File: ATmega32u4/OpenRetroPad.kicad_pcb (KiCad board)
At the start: 2 copper layers, 46 x 74 mm, 45 parts, among them J1 USB_B_Micro, J2 NRF24, J3 DB25_Female_MountingHoles, SW1 SW_Push, SW2 SW_Push, U1 ATmega32U4, U2 AMS1117-3.3, Y1 16MHz

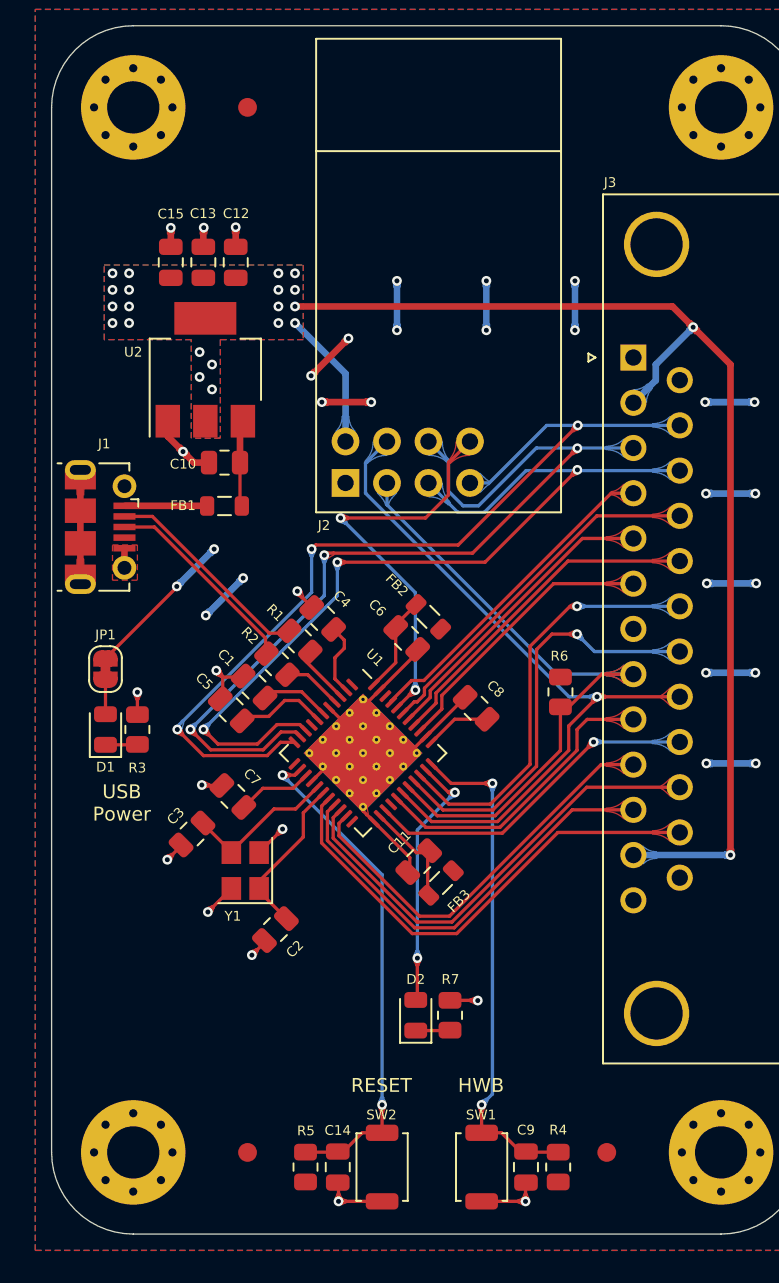
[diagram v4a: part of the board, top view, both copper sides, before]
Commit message: - Add on-board programmer - Micro USB -> USB-C
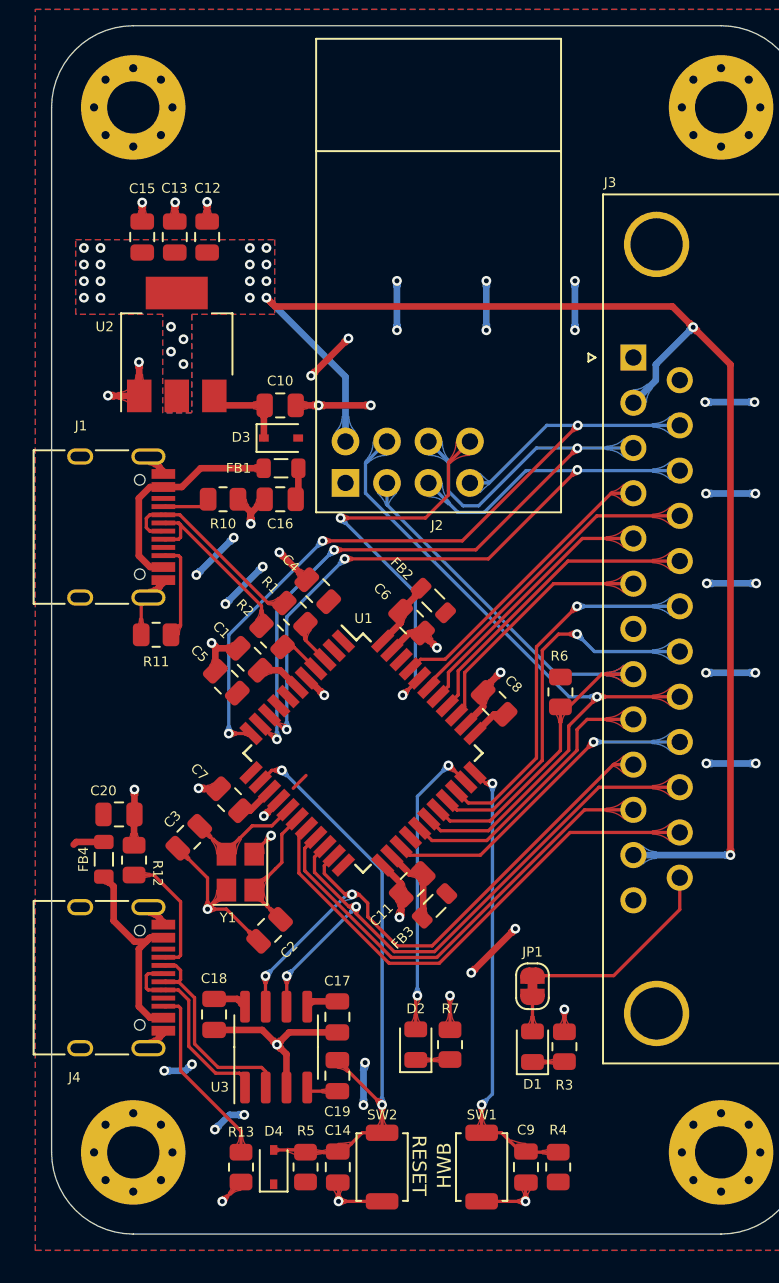
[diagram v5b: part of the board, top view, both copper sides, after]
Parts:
- removed FID1, FID2, FID3: Fiducial, OpenRetroPad:Fiducial_JLCPCB
- added C16: 10u, Capacitor_SMD:C_0805_2012Metric, F.Cu at (120.8, 86.2)
- added C17: 100n, Capacitor_SMD:C_0805_2012Metric, F.Cu at (124.3, 117.9)
- added C18: 100n, Capacitor_SMD:C_0805_2012Metric, F.Cu at (116.7, 117.8)
- added C19: 100n, Capacitor_SMD:C_0805_2012Metric, F.Cu at (124.3, 121.5)
- added C20: 10u, Capacitor_SMD:C_0805_2012Metric, F.Cu at (110.9, 105.5)
- added D3: 1N5817, Diode_SMD:D_SOD-323, F.Cu at (120.8, 82.5)
- added D4: 1N5817, Diode_SMD:D_SOD-323, F.Cu at (120.4, 127.1)
- added FB4: 500mA, Inductor_SMD:L_0805_2012Metric, F.Cu at (110.0, 108.3)
- added J4: USB_C_Receptacle_USB2.0, Connector_USB:USB_C_Receptacle_HRO_TYPE-C-31-M-12, F.Cu at (109.6, 115.5)
- added R10: 5.1k, Resistor_SMD:R_0805_2012Metric, F.Cu at (117.3, 86.2)
- added R11: 5.1k, Resistor_SMD:R_0805_2012Metric, F.Cu at (113.2, 94.5)
- added R12: 5.1k, Resistor_SMD:R_0805_2012Metric, F.Cu at (111.8, 108.3)
- added R13: 5.1k, Resistor_SMD:R_0805_2012Metric, F.Cu at (118.4, 127.1)
- added U3: CH330N, Package_SO:SOIC-8_3.9x4.9mm_P1.27mm, F.Cu at (120.5, 119.8)
- J1: value USB_B_Micro -> USB_C_Receptacle_USB2.0; footprint OpenRetroPad:105017-0001 -> Connector_USB:USB_C_Receptacle_HRO_TYPE-C-31-M-12
- U1: footprint Package_DFN_QFN:QFN-44-1EP_7x7mm_P0.5mm_EP5.15x5.15mm_ThermalVias -> Package_QFP:TQFP-44_10x10mm_P0.8mm
- moved JP1 32.6 mm to (136.2, 116.1)
- moved D1 32.6 mm to (136.2, 119.8)
- moved R3 32.6 mm to (138.2, 119.8)
- moved C10 4.89 mm to (120.8, 80.5), turned to 180 degrees
- moved FB1 4.16 mm to (120.8, 84.3)
- moved C12 2.34 mm to (116.3, 70.2)
- moved C13 2.34 mm to (114.3, 70.2)
- moved C15 2.34 mm to (112.3, 70.2)
- moved U2 2.34 mm to (114.4, 76.8)
- moved D2 1.80 mm to (129.1, 119.6)
- moved R7 1.80 mm to (131.2, 119.6)
- moved C1 1.73 mm to (118.9, 96.0)
- moved C4 1.73 mm to (123.1, 91.8)
- moved R1 1.73 mm to (121.7, 93.2)
- moved R2 1.73 mm to (120.3, 94.6)
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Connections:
- C10 pad 2: +5V -> Net-(C10-Pad2)
- R1 pad 2: D- -> MCU_D-
- R2 pad 2: D+ -> MCU_D+
- U2 pad 3: +5V -> Net-(C10-Pad2)
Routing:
- net GND: track 73.9 -> 92.9 mm, vias 19 -> 29
- net /UART_D-: track 0.00 -> 14.0 mm
- net D-: track 13.1 -> 0.00 mm
- net Net-(FB4-Pad2): track 0.00 -> 12.9 mm
- net D+: track 12.5 -> 0.00 mm
- net MCU_D-: track 0.00 -> 12.5 mm
- net /UART_D+: track 0.00 -> 12.4 mm
- net Net-(J4-PadB5): track 0.00 -> 11.5 mm
- net MCU_D+: track 0.00 -> 11.4 mm
- net PD3: track 25.3 -> 36.4 mm, vias 0 -> 2
- net PD2: track 28.7 -> 38.5 mm, vias 0 -> 2
- net Net-(FB1-Pad2): track 5.04 -> 14.1 mm
- net PB2: track 56.9 -> 48.7 mm
- net PB1: track 55.2 -> 47.0 mm
- net PB3: track 56.4 -> 48.4 mm
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- removed copper zone on F.Cu, net GND
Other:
- board text added: "OpenRetroPad ATmega32u4 v1 MAY-2021 OpenRetroPad.com JLCJLCJLCJLC"
- board text removed: "- - - D14 D16 D15 D23 D21 D20 D19 D18 D5 - D10 D9 D8 D6 D4 D1 D0 D2 D3 - - -"
- board text removed: "- - - MISO MOSI SCK A5 A3 A2 A1 A0 - - A10 A9 A8 A7 A6 TX RX SDA SCL - - -"
- board text removed: "Alt"
- board text removed: "Leonardo"
- board text removed: "OpenRetroPad ATmega32u4 v1 JAN-2021 OpenRetroPad.com"
- board text removed: "USB Power"

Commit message: Update V2
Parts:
- added D5: 1N5817, Diode_SMD:D_SOD-323, F.Cu at (105.5, 141.5)
- added D6: Power, LED_SMD:LED_0603_1608Metric, F.Cu at (98.2, 138.7)
- added D7: RX, LED_SMD:LED_0603_1608Metric, F.Cu at (121.9, 154.4)
- added D8: TX, LED_SMD:LED_0603_1608Metric, F.Cu at (123.5, 154.4)
- added F1: 500mA, Fuse:Fuse_0805_2012Metric, F.Cu at (121.6, 109.2)
- added F2: 500mA, Fuse:Fuse_0805_2012Metric, F.Cu at (121.6, 113.5)
- added R14: 1k, Resistor_SMD:R_0603_1608Metric, F.Cu at (121.9, 150.0)
- added R15: 1k, Resistor_SMD:R_0603_1608Metric, F.Cu at (123.5, 150.0)
- added R16: 330, Resistor_SMD:R_0603_1608Metric, F.Cu at (115.5, 161.4)
- added R8: 1k, Resistor_SMD:R_0603_1608Metric, F.Cu at (118.3, 150.0)
- added R9: 330, Resistor_SMD:R_0603_1608Metric, F.Cu at (120.5, 161.4)
- added U4: USBLC6-2SC6, Package_TO_SOT_SMD:SOT-23-6, F.Cu at (106.1, 126.0)
- added U5: USBLC6-2SC6, Package_TO_SOT_SMD:SOT-23-6, F.Cu at (106.0, 153.4)
- C1: value 1u -> 10u
- C10, C16, C20: value 10u -> 100n; footprint Capacitor_SMD:C_0805_2012Metric -> Capacitor_SMD:C_0603_1608Metric
- C11: value 100n -> 20pF; footprint Capacitor_SMD:C_0805_2012Metric -> Capacitor_SMD:C_0603_1608Metric
- C12: value 10u -> 20pF; footprint Capacitor_SMD:C_0805_2012Metric -> Capacitor_SMD:C_0603_1608Metric
- C13, C15, C17, C18, C19, C4, C8, C9: footprint Capacitor_SMD:C_0805_2012Metric -> Capacitor_SMD:C_0603_1608Metric
- C14, C7: value 100n -> 1u; footprint Capacitor_SMD:C_0805_2012Metric -> Capacitor_SMD:C_0603_1608Metric
- C2, C3: value 20pF -> 10u
- C5: value 1u -> 100n; footprint Capacitor_SMD:C_0805_2012Metric -> Capacitor_SMD:C_0603_1608Metric
- C6: value 100n -> 10u
- D1: value Power LED -> 1N5817; footprint LED_SMD:LED_0805_2012Metric -> Diode_SMD:D_SOD-323
- D2: value LED1 -> TX; footprint LED_SMD:LED_0805_2012Metric -> LED_SMD:LED_0603_1608Metric
- D3: value 1N5817 -> RX; footprint Diode_SMD:D_SOD-323 -> LED_SMD:LED_0603_1608Metric
- D4: value 1N5817 -> User; footprint Diode_SMD:D_SOD-323 -> LED_SMD:LED_0603_1608Metric
- FB3, FB4: footprint Inductor_SMD:L_0805_2012Metric -> Inductor_SMD:L_0603_1608Metric
- H1, H2, H3, H4: value 3.2mm_M3 -> 3.2mm M3
- J2: value NRF24 -> USB_C_Receptacle_USB2.0; footprint OpenRetroPad:NRF24L01 -> Connector_USB:USB_C_Receptacle_HRO_TYPE-C-31-M-12
- J3: value DB25_Female_MountingHoles -> NRF24; footprint Connector_Dsub:DSUB-25_Female_Horizontal_P2.77x2.84mm_EdgePinOffset7.70mm_Housed_MountingHolesOffset9.12mm -> OpenRetroPad:NRF24L01
- J4: value USB_C_Receptacle_USB2.0 -> DB25_Male_MountingHoles; footprint Connector_USB:USB_C_Receptacle_HRO_TYPE-C-31-M-12 -> Connector_Dsub:DSUB-25_Male_Horizontal_P2.77x2.84mm_EdgePinOffset7.70mm_Housed_MountingHolesOffset9.12mm
- R1, R2: value 22r -> 5.1k; footprint Resistor_SMD:R_0805_2012Metric -> Resistor_SMD:R_0603_1608Metric
- R10, R12, R13: value 5.1k -> 1k; footprint Resistor_SMD:R_0805_2012Metric -> Resistor_SMD:R_0603_1608Metric
- R11: value 5.1k -> 10k; footprint Resistor_SMD:R_0805_2012Metric -> Resistor_SMD:R_0603_1608Metric
- R3: value 1k -> 5.1k; footprint Resistor_SMD:R_0805_2012Metric -> Resistor_SMD:R_0603_1608Metric
- R4: value 10k -> 5.1k; footprint Resistor_SMD:R_0805_2012Metric -> Resistor_SMD:R_0603_1608Metric
- R5: value 10k -> 22r; footprint Resistor_SMD:R_0805_2012Metric -> Resistor_SMD:R_0603_1608Metric
- R6: value 1k -> 22r; footprint Resistor_SMD:R_0805_2012Metric -> Resistor_SMD:R_0603_1608Metric
- R7: footprint Resistor_SMD:R_0805_2012Metric -> Resistor_SMD:R_0603_1608Metric
- SW1: value SW_Push -> HWB
- SW2: value SW_Push -> RESET
- U1: value ATmega32U4 -> AMS1117-3.3; footprint Package_QFP:TQFP-44_10x10mm_P0.8mm -> Package_TO_SOT_SMD:SOT-223-3_TabPin2
- U2: value AMS1117-3.3 -> ATmega32U4-M; footprint Package_TO_SOT_SMD:SOT-223-3_TabPin2 -> Package_QFP:TQFP-44_10x10mm_P0.8mm
- moved H2 112.4 mm to (100.0, 164.0)
- moved C15 79.9 mm to (115.2, 150.0), turned to 90 degrees
- moved C12 74.0 mm to (107.7, 143.7), turned to -135 degrees
- moved J2 73.2 mm to (97.8, 153.3), turned to -90 degrees
- moved D3 72.0 mm to (118.3, 154.4), turned to -90 degrees
- moved C16 65.0 mm to (108.2, 150.0), turned to 90 degrees
- moved C10 64.4 mm to (122.5, 144.9), turned to 135 degrees
- moved FB2 63.0 mm to (104.0, 149.7), turned to 90 degrees
- moved C13 60.6 mm to (110.4, 130.7), turned to -45 degrees
- moved U2 59.4 mm to (118.0, 136.0), turned to -45 degrees
- moved C6 59.1 mm to (103.0, 146.9), turned to 0 degrees
- moved R10 56.1 mm to (125.6, 141.8), turned to 135 degrees
- moved J3 53.9 mm to (112.9, 122.7)
- moved R3 49.7 mm to (104.6, 156.4), turned to 0 degrees
- moved LOGO1 46.3 mm to (109.1, 164.1)
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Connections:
- C1 pad 2: Net-(C1-Pad2) -> +5V
- C10 pad 2: Net-(C10-Pad2) -> /Microcontroller/AVCC_P24
- C11 pad 1: GND -> /Microcontroller/XTAL1
- C11 pad 2: Net-(C11-Pad2) -> GND
- C12 pad 1: GND -> /Microcontroller/XTAL2
- C12 pad 2: +3V3 -> GND
- C13 pad 2: +3V3 -> /Microcontroller/UCAP
- C14 pad 1: RESET -> GND
- C14 pad 2: GND -> /Microcontroller/UGND
- C15 pad 2: +3V3 -> +5V
- C16 pad 2: +5V -> /UART/V3
- C17 pad 1: GND -> /UART/RTS
- C17 pad 2: +5V -> /DB25/RST
- C18 pad 2: Net-(C18-Pad2) -> /Microcontroller/AVCC_P44
- C19 pad 1: Net-(C19-Pad1) -> /DB25/RST
- C19 pad 2: RESET -> GND
- C2 pad 1: XTAL1 -> GND
- C2 pad 2: GND -> /Power/VREGIN
- C3 pad 1: XTAL2 -> GND
- C3 pad 2: GND -> +3V3
- C4 pad 2: +5V -> +3V3
- C5 pad 2: +5V -> +3V3
- C6 pad 2: Net-(C6-Pad2) -> +5V
- C9 pad 1: PE2 -> GND
- C9 pad 2: GND -> +5V
- D1 pad 1: Net-(D1-Pad1) -> /Power/VREGIN
- D1 pad 2: Net-(D1-Pad2) -> +5V
- D2 pad 2: PC7 -> +5V
- D3 pad 1: Net-(C10-Pad2) -> Net-(D3-Pad1)
- D4 pad 1: +5V -> Net-(D4-Pad1)
- D4 pad 2: RESET -> /IO/LED_USER
- FB1 pad 1: +5V -> /USB Data/VBUS
- FB1 pad 2: Net-(FB1-Pad2) -> +5V
- FB2 pad 1: +5V -> /USB Program/VBUS
- FB2 pad 2: Net-(C6-Pad2) -> +5V
- FB3 pad 1: +5V -> /Microcontroller/AVCC_P24
- FB3 pad 2: Net-(C11-Pad2) -> +5V
- FB4 pad 1: +5V -> /Microcontroller/AVCC_P44
- FB4 pad 2: Net-(FB4-Pad2) -> +5V
- H1 pad 1: (no net) -> unconnected-(H1-Pad1)
- H2 pad 1: (no net) -> unconnected-(H2-Pad1)
- H3 pad 1: (no net) -> unconnected-(H3-Pad1)
- H4 pad 1: (no net) -> unconnected-(H4-Pad1)
- J1 pad A4: Net-(FB1-Pad2) -> /USB Data/VBUS
- J1 pad A5: Net-(J1-PadA5) -> /USB Data/CC1
- J1 pad A6: MCU_D+ -> /USB Data/D+
- J1 pad A7: MCU_D- -> /USB Data/D-
- J1 pad A8: Net-(J1-PadA8) -> unconnected-(J1-PadA8)
- J1 pad A9: Net-(FB1-Pad2) -> /USB Data/VBUS
- J1 pad B4: Net-(FB1-Pad2) -> /USB Data/VBUS
- J1 pad B5: Net-(J1-PadB5) -> /USB Data/CC2
- J1 pad B6: MCU_D+ -> /USB Data/D+
- J1 pad B7: MCU_D- -> /USB Data/D-
- J1 pad B8: Net-(J1-PadB8) -> unconnected-(J1-PadB8)
- J1 pad B9: Net-(FB1-Pad2) -> /USB Data/VBUS
- J3 pad 3: PB2 -> /DB25/CE
- J3 pad 4: PF0 -> /DB25/CSN
- J3 pad 5: PF5 -> /DB25/SCK
- J3 pad 6: PF7 -> /DB25/MOSI
- J3 pad 7: Net-(J3-Pad7) -> /DB25/MISO
- J3 pad 8: PB5 -> /DB25/IRQ
- JP1 pad 2: Net-(D1-Pad2) -> Net-(D6-Pad2)
- R1 pad 1: Net-(R1-Pad1) -> /USB Data/CC2
- R1 pad 2: MCU_D- -> GND
- R10 pad 2: Net-(J1-PadA5) -> Net-(D4-Pad1)
- R11 pad 1: Net-(J1-PadB5) -> +5V
- R11 pad 2: GND -> /DB25/RST
- R12 pad 1: GND -> /DB25/PB5
- R12 pad 2: Net-(J4-PadA5) -> +5V
- R13 pad 1: Net-(J4-PadB5) -> Net-(D6-Pad1)
- R2 pad 1: Net-(R2-Pad1) -> GND
- R2 pad 2: MCU_D+ -> /USB Data/CC1
- R3 pad 1: Net-(D1-Pad1) -> /USB Program/CC2
- R4 pad 1: +5V -> GND
- R4 pad 2: PE2 -> /USB Program/CC1
- R5 pad 1: +5V -> /Microcontroller/D+
- R5 pad 2: RESET -> /Microcontroller/USB_DATA.DP
- R6 pad 1: PB5 -> /Microcontroller/D-
- R6 pad 2: +5V -> /Microcontroller/USB_DATA.DM
- R7 pad 1: GND -> Net-(D2-Pad1)
- R7 pad 2: Net-(D2-Pad1) -> /DB25/TX
- SW1 pad 1: PE2 -> Net-(R9-Pad2)
- SW2 pad 1: RESET -> Net-(R16-Pad2)
- U1 pad 1: Net-(U1-Pad1) -> GND
- U1 pad 2: +5V -> +3V3
- U1 pad 3: Net-(R1-Pad1) -> /Power/VREGIN
- U2 pad 1: GND -> /DB25/CE
- U2 pad 2: +3V3 -> +5V
- U2 pad 3: Net-(C10-Pad2) -> /Microcontroller/D-
- U3 pad 1: /UART_D+ -> /UART/USB_PRGM.DP
- U3 pad 2: /UART_D- -> /UART/USB_PRGM.DM
- U3 pad 4: Net-(C19-Pad1) -> /UART/RTS
- U3 pad 6: PD2 -> /DB25/TX
- U3 pad 7: PD3 -> /DB25/RX
- U3 pad 8: Net-(C18-Pad2) -> /UART/V3
- Y1 pad 1: XTAL1 -> /Microcontroller/XTAL1
- Y1 pad 3: XTAL2 -> /Microcontroller/XTAL2
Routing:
- net +3V3: track 83.6 -> 30.2 mm, vias 22 -> 26
- net PB2: track 48.7 -> 0.00 mm, vias 3 -> 0
- net PB3: track 48.4 -> 0.00 mm, vias 3 -> 0
- net PB1: track 47.0 -> 0.00 mm, vias 3 -> 0
- net /DB25/MISO: track 0.00 -> 45.7 mm, vias 0 -> 2
- net /DB25/RX: track 0.00 -> 43.7 mm, vias 0 -> 1
- net PB4: track 43.0 -> 0.00 mm, vias 1 -> 0
- net /DB25/MOSI: track 0.00 -> 42.1 mm, vias 0 -> 1
- net /DB25/SCK: track 0.00 -> 39.7 mm, vias 0 -> 1
- net PD2: track 38.5 -> 0.00 mm, vias 2 -> 0
- net PB5: track 38.3 -> 0.00 mm
- net RESET: track 37.7 -> 0.00 mm, vias 2 -> 0
- net /DB25/RST: track 0.00 -> 37.6 mm, vias 0 -> 4
- net PD3: track 36.4 -> 0.00 mm, vias 2 -> 0
- net /DB25/TX: track 0.00 -> 32.4 mm, vias 0 -> 3
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- added copper zone on In2.Cu, net +5V
- added copper zone on F.Cu, net GND
- added copper zone on In1.Cu, net GND
- removed copper zone on B.Cu, net GND
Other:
- copper layers 2 -> 4
- net class Default removed
- board text added: "DATA"
- board text added: "OpenRetroPad ATmega32u4 v2 DEC-2022 OpenRetroPad.com JLCJLCJLCJLC"
- board text added: "POWER"
- board text added: "PRGM"
- board text added: "RX TX"
- board text added: "TX RX"
- board text added: "UART"
- board text added: "USB"
- board text added: "USER"
- board text removed: "1 14 2 15 3 16 4 17 5 18 6 19 7 20 8 21 9 22 10 23 11 24 12 25 13"
- board text removed: "3V3 GND"
- board text removed: "ATmega32u4"
- board text removed: "DB25"
- board text removed: "GND 5V 3V3 PB3 PB2 PB1 PF0 PF4 PF5 PF6 PF7 PC6 - PB6 PB5 PB4 PD7 PD4 PD3 PD2 PD1 PD0 3V3 5V GND"
- board text removed: "OpenRetroPad ATmega32u4 v1 MAY-2021 OpenRetroPad.com JLCJLCJLCJLC"
- board text removed: "PB2 PB1"
- board text removed: "PB4 PB5"
- board text removed: "PF1 PB3"

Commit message: Update layout/assembly pdf
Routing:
- net /DB25/PD0: track 28.9 -> 27.5 mm
- net /Microcontroller/USB_DATA.DP: track 5.14 -> 6.22 mm
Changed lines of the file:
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@@
   (segment (start 116.15 143.506854) (end 116.797918 142.858936) (width 0.2032) (layer "F.Cu") (net 17))
   (segment (start 123.017053 149.175) (end 121.492053 147.65) (width 0.2032) (layer "F.Cu") (net 17))
-  (segment (start 110.928678 126.95) (end 111.955976 127.977298) (width 0.2032) (layer "F.Cu") (net 20))
-  (segment (start 107.2375 126.95) (end 110.928678 126.95) (width 0.2032) (layer "F.Cu") (net 20))
-  (segment (start 107.2375 125.05) (end 111.15 125.05) (width 0.2032) (layer "F.Cu") (net 21))
-  (segment (start 111.15 125.05) (end 113.016637 126.916637) (width 0.2032) (layer "F.Cu") (net 21))
+  (segment (start 108.271342 126.2) (end 110.95 126.2) (width 0.2032) (layer "F.Cu") (net 20))
+  (segment (start 110.95 126.2) (end 111.955976 127.205976) (width 0.2032) (layer "F.Cu") (net 20))
+  (segment (start 107.521342 126.95) (end 108.271342 126.2) (width 0.2032) (layer "F.Cu") (net 20))
+  (segment (start 111.955976 127.205976) (end 111.955976 127.977298) (width 0.2032) (layer "F.Cu") (net 20))
+  (segment (start 107.2375 126.95) (end 107.521342 126.95) (width 0.2032) (layer "F.Cu") (net 20))
+  (segment (start 108.221342 125.75) (end 111.1 125.75) (width 0.2032) (layer "F.Cu") (net 21))
+  (segment (start 112.266637 126.916637) (end 113.016637 126.916637) (width 0.2032) (layer "F.Cu") (net 21))
+  (segment (start 107.521342 125.05) (end 108.221342 125.75) (width 0.2032) (layer "F.Cu") (net 21))
+  (segment (start 107.2375 125.05) (end 107.521342 125.05) (width 0.2032) (layer "F.Cu") (net 21))
+  (segment (start 111.1 125.75) (end 112.266637 126.916637) (width 0.2032) (layer "F.Cu") (net 21))
   (segment (start 116.7 150.825) (end 116.7 153.6125) (width 0.2032) (layer "F.Cu") (net 22))
-  (segment (start 107.1375 154.35) (end 109.795 154.35) (width 0.2032) (layer "F.Cu") (net 23))
-  (segment (start 109.795 154.35) (end 109.795 154.675) (width 0.2032) (layer "F.Cu") (net 23))
-  (segment (start 111.065 154.015) (end 111.065 154.675) (width 0.2032) (layer "F.Cu") (net 24))
-  (segment (start 107.1375 152.45) (end 109.5 152.45) (width 0.2032) (layer "F.Cu") (net 24))
-  (segment (start 109.5 152.45) (end 111.065 154.015) (width 0.2032) (layer "F.Cu") (net 24))
+  (segment (start 109.795 154.15) (end 109.795 154.675) (width 0.2032) (layer "F.Cu") (net 23))
+  (segment (start 107.1375 154.35) (end 107.3375 154.15) (width 0.2032) (layer "F.Cu") (net 23))
+  (segment (start 107.3375 154.15) (end 109.795 154.15) (width 0.2032) (layer "F.Cu") (net 23))
+  (segment (start 111.065 154.065) (end 111.065 154.675) (width 0.2032) (layer "F.Cu") (net 24))
+  (segment (start 108.896 153.446) (end 110.446 153.446) (width 0.2032) (layer "F.Cu") (net 24))
+  (segment (start 107.1375 152.45) (end 107.9 152.45) (width 0.2032) (layer "F.Cu") (net 24))
+  (segment (start 110.446 153.446) (end 111.065 154.065) (width 0.2032) (layer "F.Cu") (net 24))
+  (segment (start 107.9 152.45) (end 108.896 153.446) (width 0.2032) (layer "F.Cu") (net 24))
   (segment (start 116.75 121.45) (end 115.46 120.16) (width 0.2032) (layer "F.Cu") (net 25))
   (segment (start 122.030509 140.030509) (end 121.1 139.1) (width 0.2032) (layer "F.Cu") (net 25))
@@
   (segment (start 113.6 147.8) (end 117.4 147.8) (width 0.2032) (layer "B.Cu") (net 39))
   (segment (start 117.4 147.8) (end 119.6 150) (width 0.2032) (layer "B.Cu") (net 39))
+  (segment (start 132.1 146.4) (end 132.1 144.460331) (width 0.2032) (layer "F.Cu") (net 40))
+  (segment (start 129.5 147.2) (end 131.3 147.2) (width 0.2032) (layer "F.Cu") (net 40))
   (segment (start 131.3 147.2) (end 132.1 146.4) (width 0.2032) (layer "F.Cu") (net 40))
-  (segment (start 119.9944 147.2944) (end 121.639347 147.2944) (width 0.2032) (layer "F.Cu") (net 40))
-  (segment (start 117.9 145.2) (end 119.9944 147.2944) (width 0.2032) (layer "F.Cu") (net 40))
-  (segment (start 128.5 148.2) (end 129.5 147.2) (width 0.2032) (layer "F.Cu") (net 40))
+  (segment (start 117.9 141.2) (end 117.9 143.1) (width 0.2032) (layer "F.Cu") (net 40))
   (segment (start 115.9 139.2) (end 115.9 139.231371) (width 0.2032) (layer "F.Cu") (net 40))
-  (segment (start 122.544947 148.2) (end 128.5 148.2) (width 0.2032) (layer "F.Cu") (net 40))
   (segment (start 115.9 139.231371) (end 114.535177 140.596194) (width 0.2032) (layer "F.Cu") (net 40))
-  (segment (start 129.5 147.2) (end 131.3 147.2) (width 0.2032) (layer "F.Cu") (net 40))
-  (segment (start 117.9 141.2) (end 117.9 145.2) (width 0.2032) (layer "F.Cu") (net 40))
-  (segment (start 132.1 146.4) (end 132.1 144.460331) (width 0.2032) (layer "F.Cu") (net 40))
+  (segment (start 128.7 148) (end 129.5 147.2) (width 0.2032) (layer "F.Cu") (net 40))
   (segment (start 132.1 144.460331) (end 130.669669 143.03) (width 0.2032) (layer "F.Cu") (net 40))
-  (segment (start 121.639347 147.2944) (end 122.544947 148.2) (width 0.2032) (layer "F.Cu") (net 40))
+  (segment (start 117.9 143.1) (end 122.8 148) (width 0.2032) (layer "F.Cu") (net 40))
+  (segment (start 122.8 148) (end 128.7 148) (width 0.2032) (layer "F.Cu") (net 40))
   (via (at 117.9 141.2) (size 0.6) (drill 0.3) (layers "F.Cu" "B.Cu") (net 40))
   (via (at 115.9 139.2) (size 0.6) (drill 0.3) (layers "F.Cu" "B.Cu") (net 40))
